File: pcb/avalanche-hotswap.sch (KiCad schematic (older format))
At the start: 103 parts, among them J1 TRRS, J2 LED, J3 OLED, P1 i2c_pin, P2 i2c_pin, SW1 SW_Push, SW10 SW_Push, SW11 SW_Push, SW12 SW_Push, SW13 SW_Push, SW14 SW_Push, SW15 SW_Push, SW16 SW_Push, SW17 SW_Push, SW18 SW_Push, SW19 SW_Push, SW2 SW_Push, SW20 SW_Push, SW21 SW_Push, SW22 SW_Push, SW23 SW_Push, SW24 SW_Push, SW25 SW_Push, SW26 SW_Push, SW27 SW_Push, SW28 SW_Push, SW29 SW_Push, SW3 SW_Push, SW30 SW_Push, SW31 SW_Push, SW32 SW_Push, SW4 SW_Push, SW5 SW_Push, SW6 SW_Push, SW7 SW_Push, SW8 SW_Push, SW9 SW_Push, U1 ProMicro

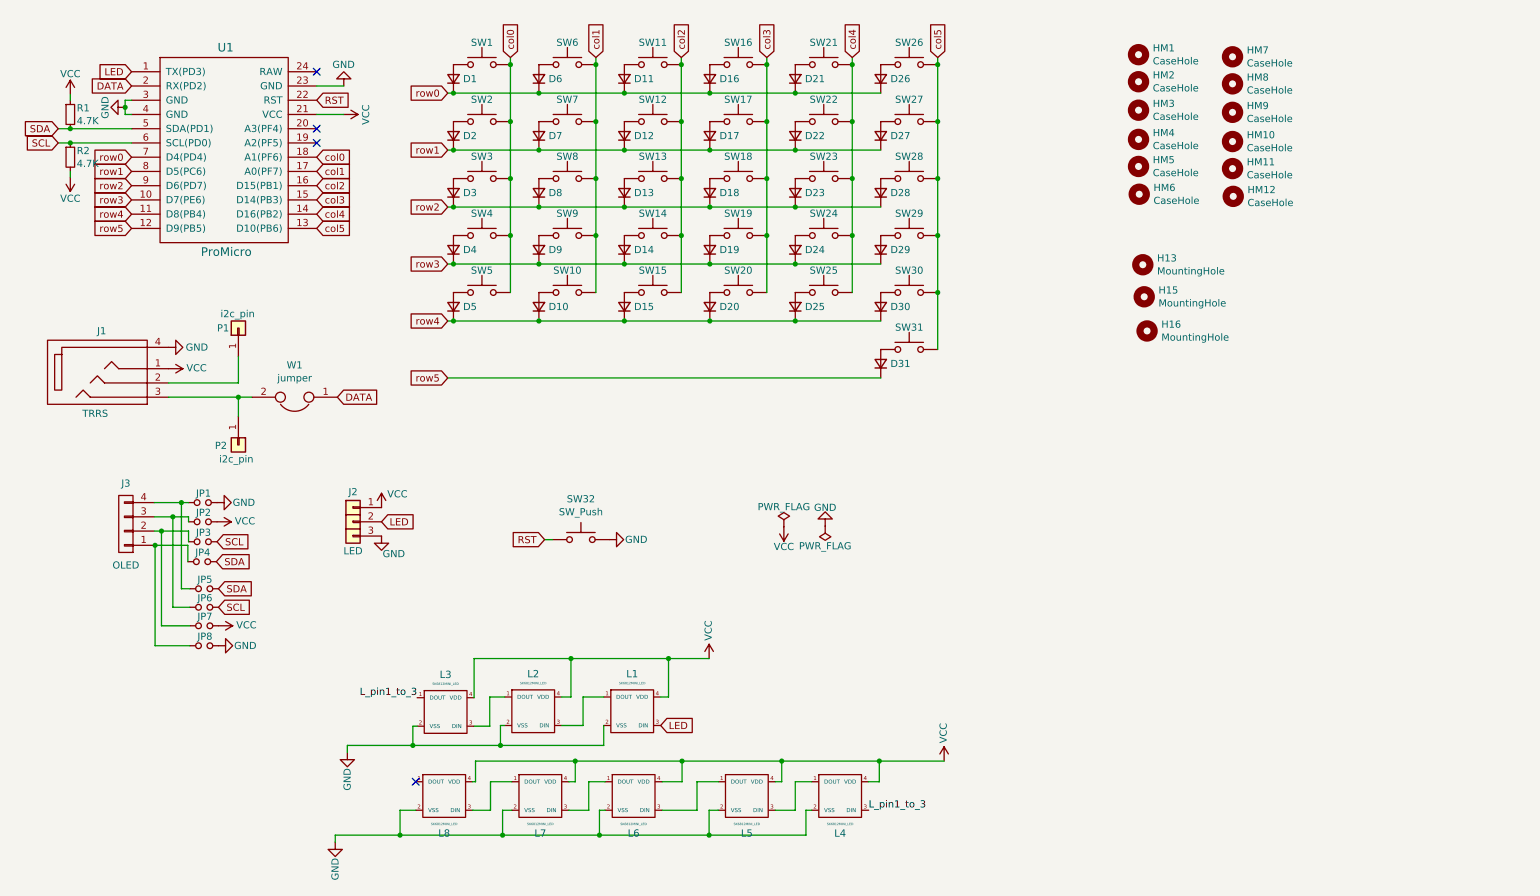
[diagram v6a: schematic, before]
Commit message: Renumbered switches and diodes.
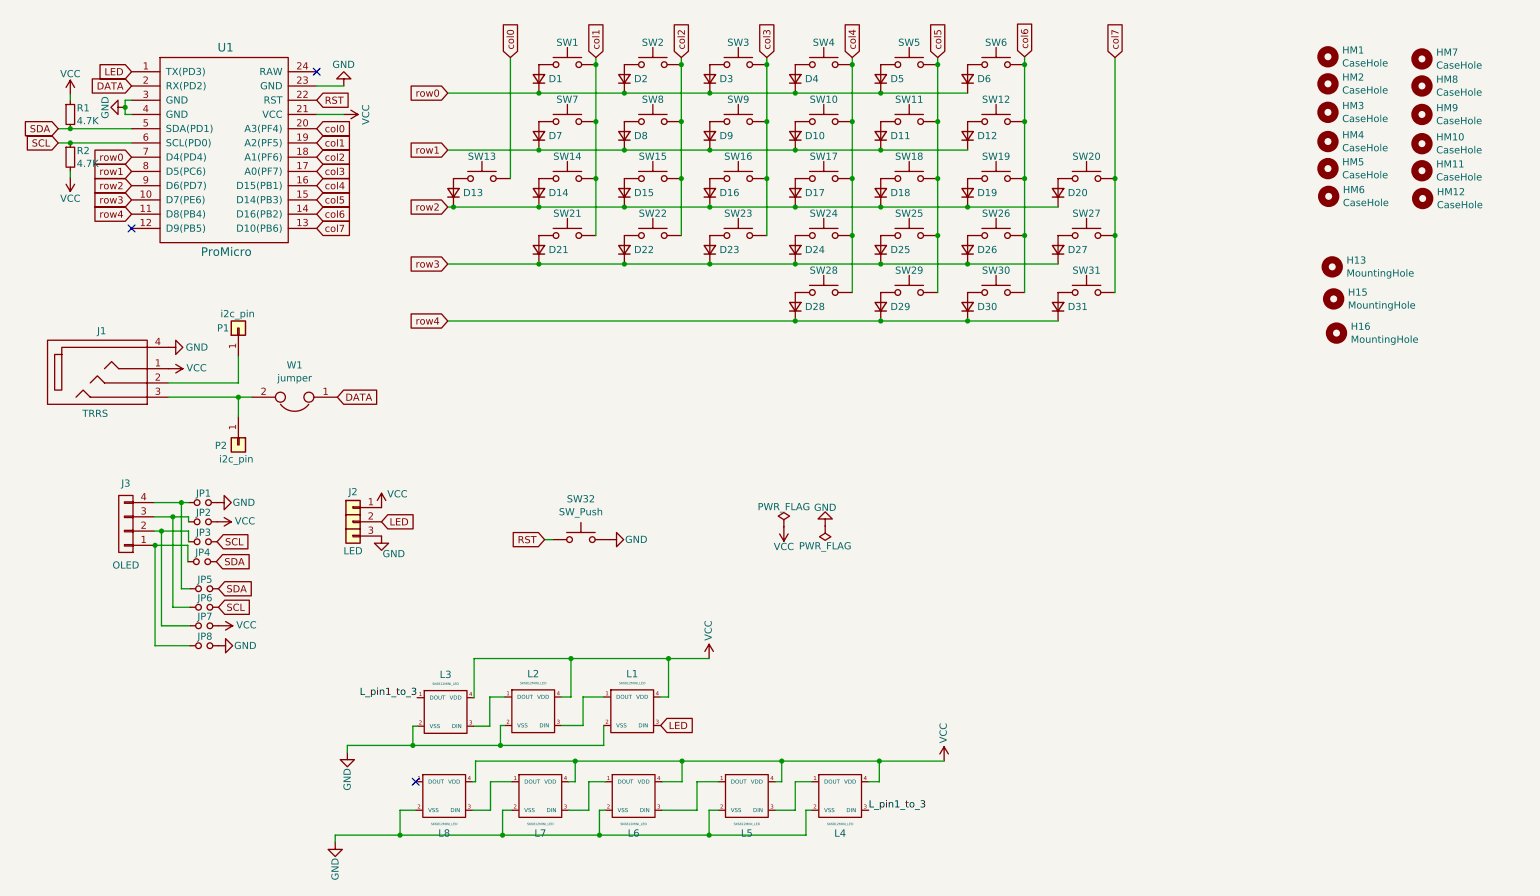
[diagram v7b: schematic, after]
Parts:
- removed D1, D10, D15, D2, D4, D5: 1N4148, used_footprints:D3_TH_SMD, symbol Device:D_Small
- removed SW1, SW2, SW4, SW5: SW_Push, used_footprints:CherryMX_MidHeight_Hotswap_1u, symbol Switch:SW_Push
- removed SW10, SW15: SW_Push, used_footprints:CherryMX_MidHeight_Hotswap_1.25u, symbol Switch:SW_Push
- added D12, D19, D26, D27, D31, D6: 1N4148, used_footprints:D3_TH_SMD, symbol Device:D_Small
- added SW12, SW19, SW26, SW27, SW31, SW6: SW_Push, used_footprints:CherryMX_MidHeight_Hotswap_1u, symbol Switch:SW_Push
- renumbered D6 to D1, D22 to D10, D27 to D11, D3 to D13, D8 to D14, D13 to D15, D18 to D16, D23 to D17, D28 to D18, D11 to D2, D9 to D21, D14 to D22, D19 to D23, D29 to D25, D25 to D28, D30 to D29, D16 to D3, D31 to D30, D21 to D4, D26 to D5, D12 to D8, D17 to D9, SW6 to SW1, SW22 to SW10, SW27 to SW11, SW3 to SW13, SW8 to SW14, SW13 to SW15, SW18 to SW16, SW23 to SW17, SW28 to SW18, SW11 to SW2, SW9 to SW21, SW14 to SW22, SW19 to SW23, SW29 to SW25, SW25 to SW28, SW30 to SW29, SW16 to SW3, SW31 to SW30, SW21 to SW4, SW26 to SW5, SW12 to SW8, SW17 to SW9
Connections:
- net col0: now also U1.20 (A3(PF4)); no longer U1.18 (A1(PF6))
- net col1: now also U1.19 (A2(PF5)); no longer U1.17 (A0(PF7))
- net col2: now also U1.18 (A1(PF6)); no longer U1.16 (D15(PB1))
- net col3: now also U1.17 (A0(PF7)); no longer SW20.2, U1.15 (D14(PB3))
- net col4: now also U1.16 (D15(PB1)); no longer U1.14 (D16(PB2))
- net col5: now also U1.15 (D14(PB3)); no longer SW30.2, U1.13 (D10(PB6))
- net row0: now also D6.1 (K)
- net row1: now also D12.1 (K)
- net row2: now also D20.1 (K), D19.1 (K)
- net row3: now also D26.1 (K), D27.1 (K)
- net row4: now also D30.1 (K), D31.1 (K); no longer D20.1 (K)
- net row5: no longer names the net of U1.12 (D9(PB5))
- net row5: no longer D30.1 (K)
- new net: D6.2 (A), SW6.1
- new net: D12.2 (A), SW12.1
- new net: D19.2 (A), SW19.1
- new net: D26.2 (A), SW26.1
- new net: D27.2 (A), SW27.1
- new net: D31.2 (A), SW31.1
- new net col6: SW12.2, SW19.2, SW26.2, SW30.2, SW6.2, U1.14 (D16(PB2))
- new net col7: SW20.2, SW27.2, SW31.2, U1.13 (D10(PB6))
- no-connect marks 4 -> 3
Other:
- moved on the sheet: D30, H13, H15, H16, HM1, HM10, HM11, HM12, HM2, HM3, HM4, HM5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

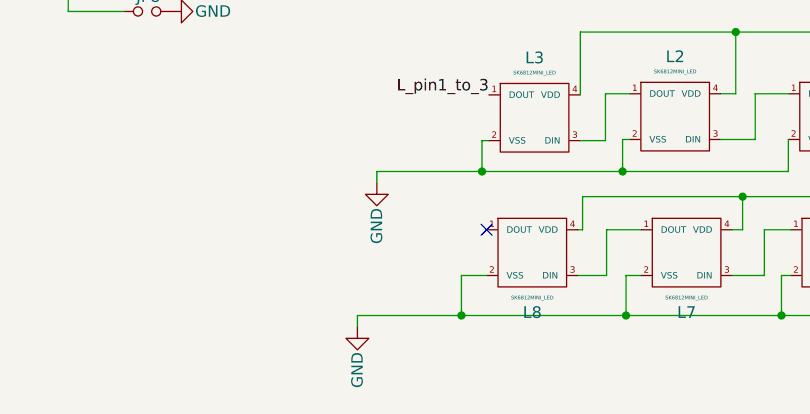
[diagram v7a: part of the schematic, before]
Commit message: Added one more underglow LED
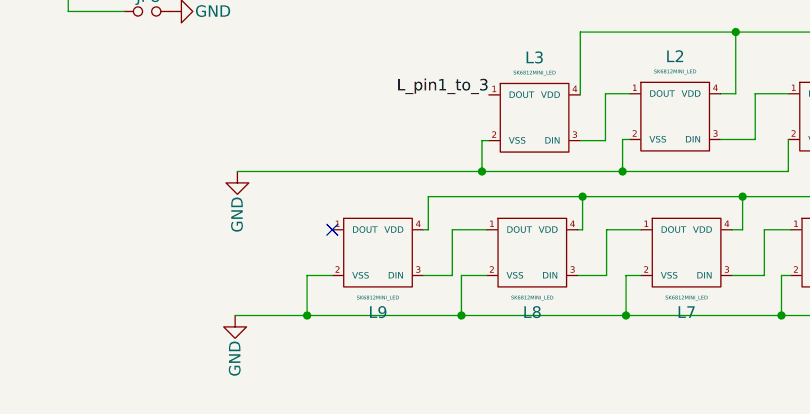
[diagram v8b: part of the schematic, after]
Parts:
- added L9: SK6812MINI_LED, used_footprints:SK6812MINI_underglow_rev, symbol avalanche-hotswap:SK6812MINI_LED
- SW28, SW29: footprint used_footprints:CherryMX_MidHeight_Hotswap_1u -> used_footprints:CherryMX_MidHeight_Hotswap_1.25u
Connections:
- net GND: now also L9.2 (VSS)
- net VCC: now also L9.4 (VDD)
- net at L8.1 (DOUT): now also L9.3 (DIN)
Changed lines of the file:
@@
 F 0 "SW28" H 6145 2645 50  0000 C CNN
 F 1 "SW_Push" H 6145 2684 50  0001 C CNN
-F 2 "used_footprints:CherryMX_MidHeight_Hotswap_1u" H 6145 2690 50  0001 C CNN
+F 2 "used_footprints:CherryMX_MidHeight_Hotswap_1.25u" H 6145 2690 50  0001 C CNN
 F 3 "~" H 6145 2690 50  0001 C CNN
 	1    6145 2490
@@
 F 0 "SW29" H 6745 2645 50  0000 C CNN
 F 1 "SW_Push" H 6745 2684 50  0001 C CNN
-F 2 "used_footprints:CherryMX_MidHeight_Hotswap_1u" H 6745 2690 50  0001 C CNN
+F 2 "used_footprints:CherryMX_MidHeight_Hotswap_1.25u" H 6745 2690 50  0001 C CNN
 F 3 "~" H 6745 2690 50  0001 C CNN
 	1    6745 2490
@@
 L power:GND #PWR0108
 U 1 1 605AF8A2
-P 2800 5720
-F 0 "#PWR0108" H 2800 5470 50  0001 C CNN
-F 1 "GND" V 2800 5610 50  0000 R CNN
-F 2 "" H 2800 5720 50  0001 C CNN
-F 3 "" H 2800 5720 50  0001 C CNN
-	1    2800 5720
-	1    0    0    -1
-$EndComp
-Wire Wire Line
-	2800 5720 2800 5670
-Wire Wire Line
-	2800 5670 3260 5670
+P 2190 5670
+F 0 "#PWR0108" H 2190 5420 50  0001 C CNN
+F 1 "GND" V 2190 5560 50  0000 R CNN
+F 2 "" H 2190 5670 50  0001 C CNN
+F 3 "" H 2190 5670 50  0001 C CNN
+	1    2190 5670
+	1    0    0    -1
+$EndComp
 Wire Wire Line
 	4600 5670 4600 5530
@@
 L power:GND #PWR0110
 U 1 1 60493A43
-P 2715 6350
-F 0 "#PWR0110" H 2715 6100 50  0001 C CNN
-F 1 "GND" V 2715 6240 50  0000 R CNN
-F 2 "" H 2715 6350 50  0001 C CNN
-F 3 "" H 2715 6350 50  0001 C CNN
-	1    2715 6350
-	1    0    0    -1
-$EndComp
-Wire Wire Line
-	2715 6350 2715 6300
-Wire Wire Line
-	2715 6300 3170 6300
+P 2180 6300
+F 0 "#PWR0110" H 2180 6050 50  0001 C CNN
+F 1 "GND" V 2180 6190 50  0000 R CNN
+F 2 "" H 2180 6300 50  0001 C CNN
+F 3 "" H 2180 6300 50  0001 C CNN
+	1    2180 6300
+	1    0    0    -1
+$EndComp
 Wire Wire Line
 	3260 5670 3875 5670
@@
 Wire Wire Line
 	3170 6300 3890 6300
-NoConn ~ 3280 5925
 Text Label 3290 5335 2    50   ~ 0
 L_pin1_to_3
@@
 Wire Wire Line
 	3505 2690 5945 2690
+Wire Wire Line
+	2190 5670 3260 5670
+Wire Wire Line
+	2180 6300 2495 6300
+$Comp
+L avalanche-hotswap:SK6812MINI_LED L9
+U 1 1 604BE742
+P 2805 6025
+F 0 "L9" H 2805 5763 51  0000 C CNN
+F 1 "SK6812MINI_LED" H 2805 5828 16  0000 C CNN
+F 2 "used_footprints:SK6812MINI_underglow_rev" H 2805 6025 60  0001 C CNN
+F 3 "" H 2805 6025 60  0001 C CNN
+	1    2805 6025
+	1    0    0    -1
+$EndComp
+Wire Wire Line
+	3280 5925 3130 5925
+Wire Wire Line
+	3130 5925 3130 6125
+Wire Wire Line
+	3130 6125 3005 6125
+Wire Wire Line
+	3005 5925 3025 5925
+Wire Wire Line
+	3025 5780 3025 5925
+Wire Wire Line
+	2605 6125 2495 6125
+NoConn ~ 2605 5925
+Wire Wire Line
+	3700 5780 3025 5780
+Connection ~ 3700 5780
+Wire Wire Line
+	2495 6125 2495 6300
+Connection ~ 2495 6300
+Wire Wire Line
+	2495 6300 3170 6300
 $EndSCHEMATC
